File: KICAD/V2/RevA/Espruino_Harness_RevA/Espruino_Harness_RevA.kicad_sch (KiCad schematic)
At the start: 0 parts

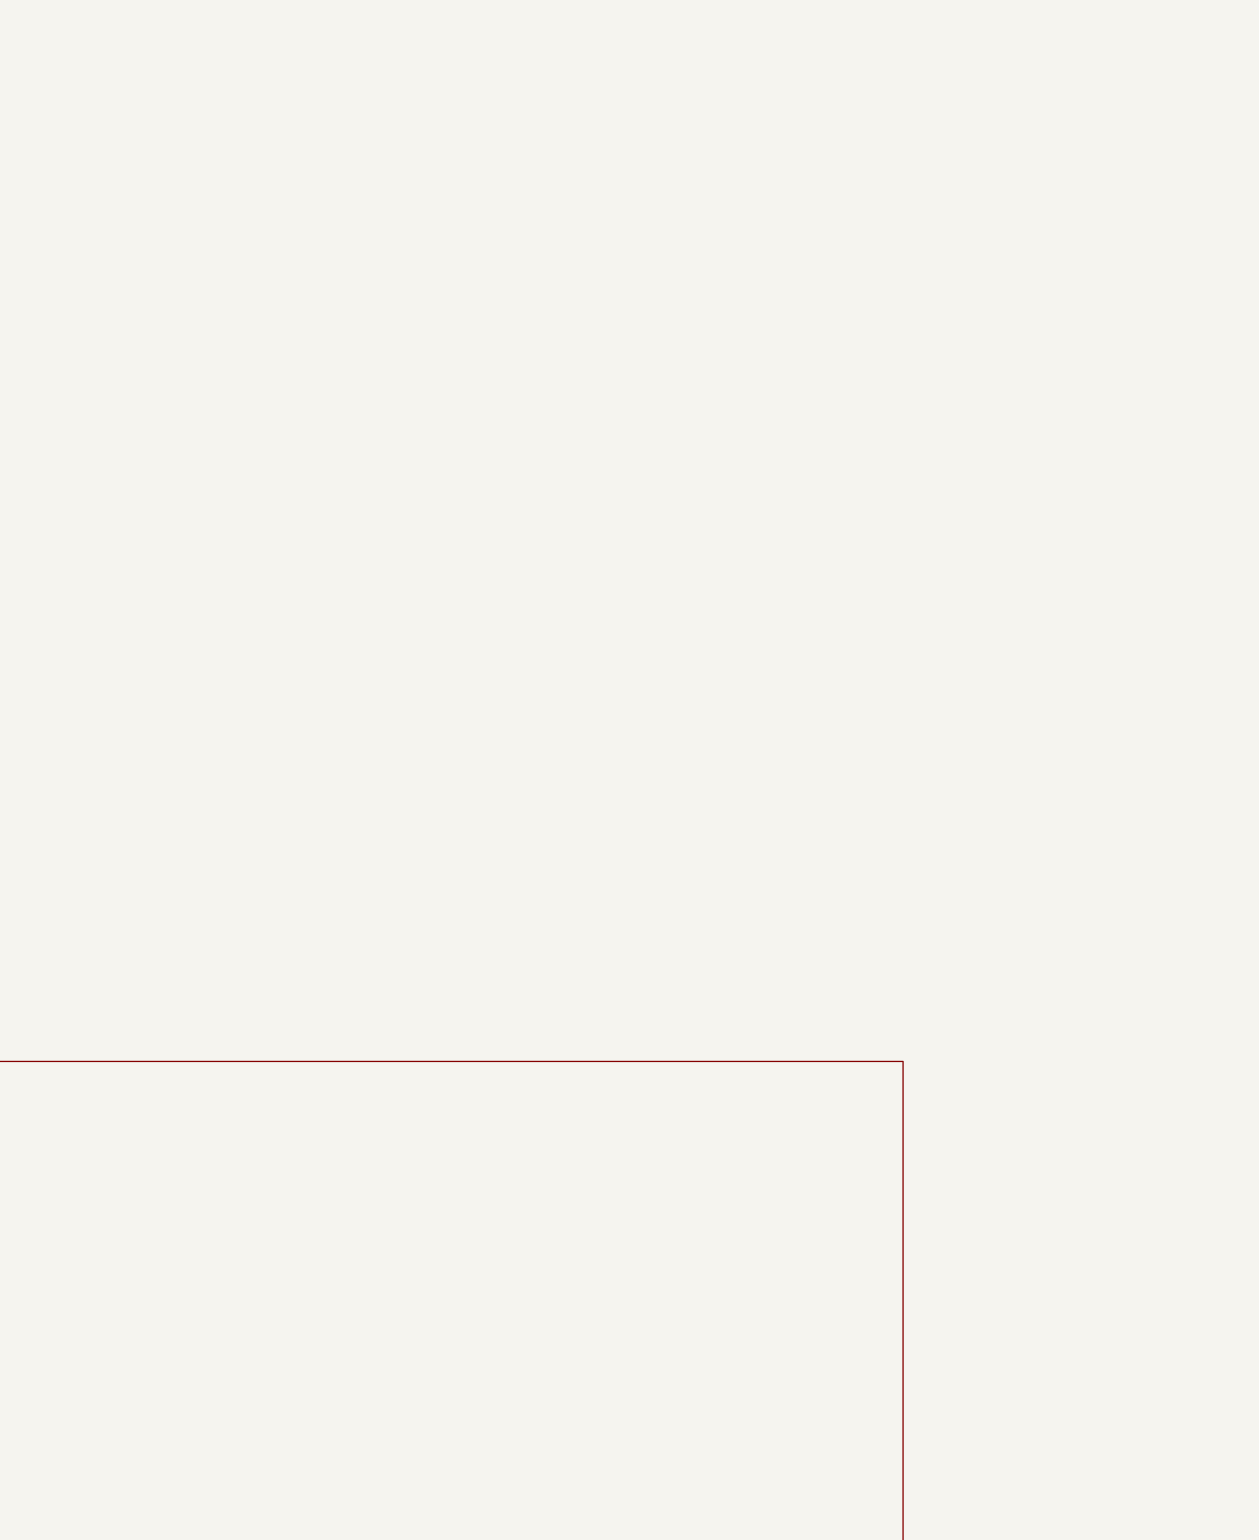
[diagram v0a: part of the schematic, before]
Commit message: Implement Target Interface and GPIO loopback
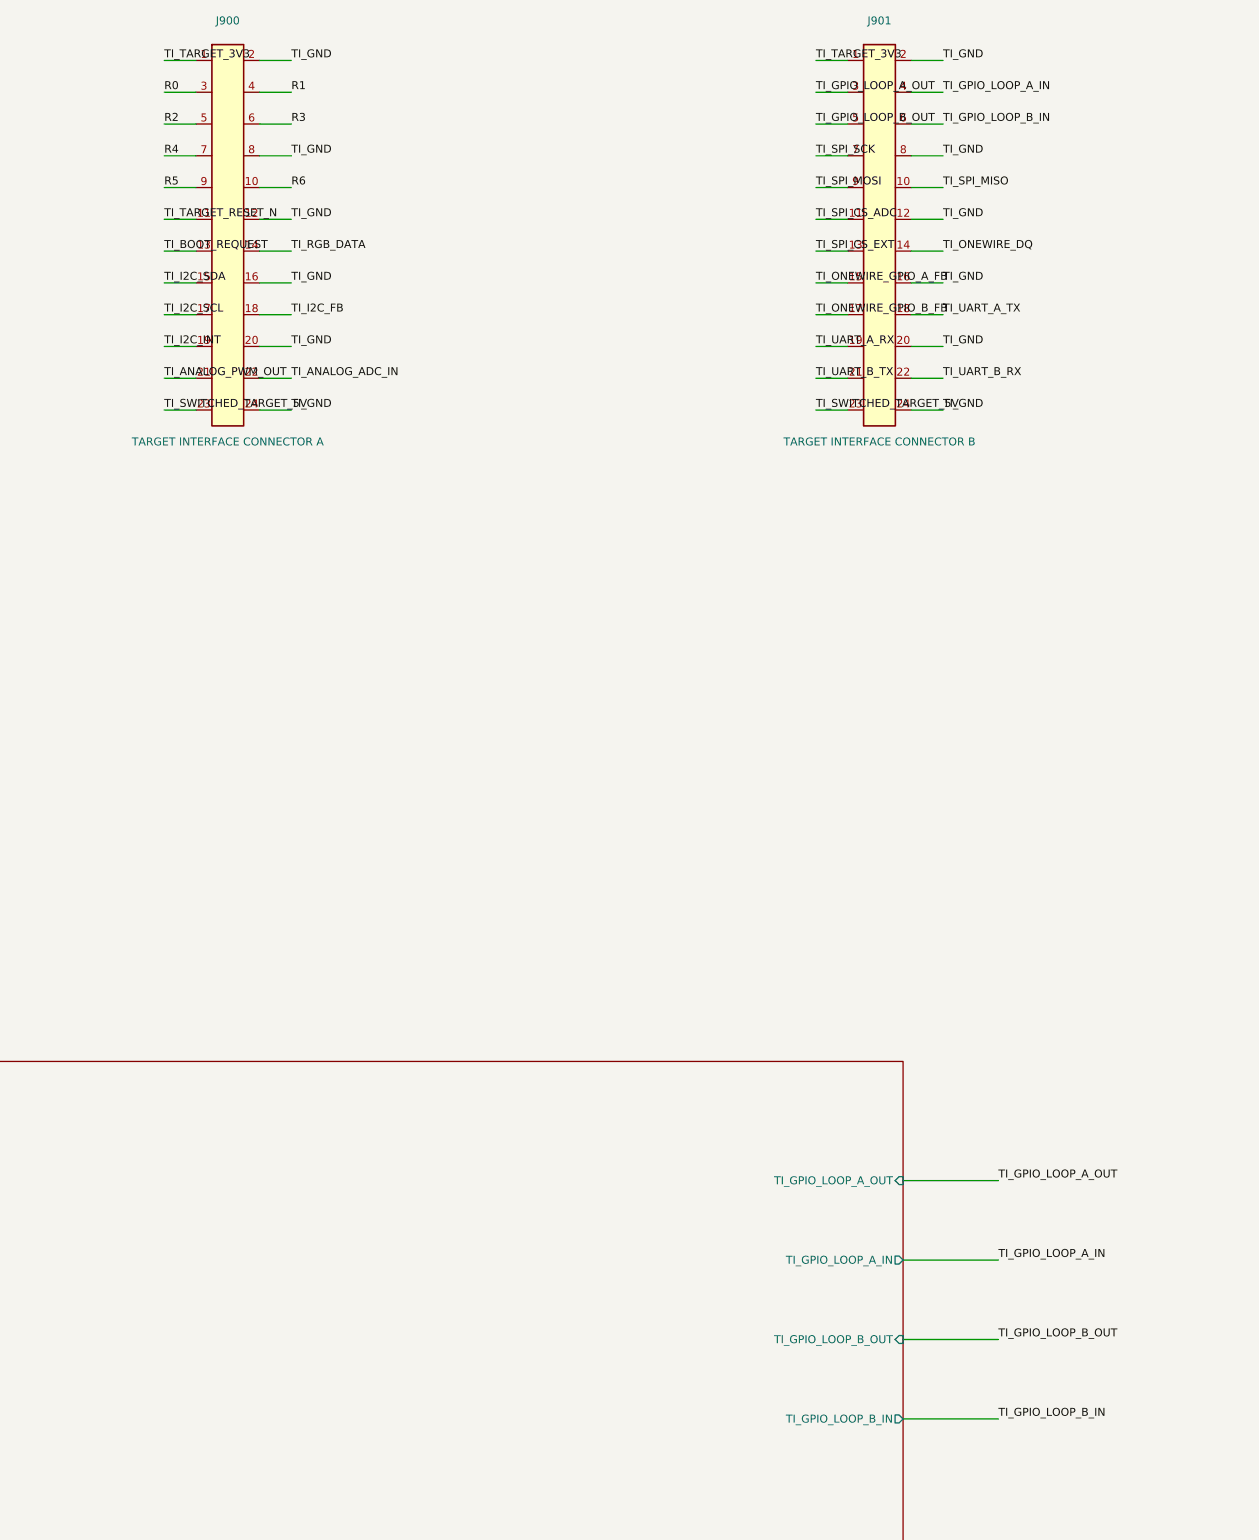
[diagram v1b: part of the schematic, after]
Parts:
- added J900: TARGET INTERFACE CONNECTOR A, symbol Espruino_Harness_RevA:Target_Interface_2x12_Odd_Even
- added J901: TARGET INTERFACE CONNECTOR B, symbol Espruino_Harness_RevA:Target_Interface_2x12_Odd_Even
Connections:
- new net R0: J900.3 (Contact_03)
- new net R1: J900.4 (Contact_04)
- new net R2: J900.5 (Contact_05)
- new net R3: J900.6 (Contact_06)
- new net R4: J900.7 (Contact_07)
- new net R5: J900.9 (Contact_09)
- new net R6: J900.10 (Contact_10)
- new net TI_ANALOG_ADC_IN: J900.22 (Contact_22)
- new net TI_ANALOG_PWM_OUT: J900.21 (Contact_21)
- new net TI_BOOT_REQUEST: J900.13 (Contact_13)
- new net TI_GND: J900.12 (Contact_12), J900.16 (Contact_16), J900.2 (Contact_02), J900.20 (Contact_20), J900.24 (Contact_24), J900.8 (Contact_08), J901.12 (Contact_12), J901.16 (Contact_16), J901.2 (Contact_02), J901.20 (Contact_20), J901.24 (Contact_24), J901.8 (Contact_08)
- new net TI_GPIO_LOOP_A_IN: J901.4 (Contact_04)
- new net TI_GPIO_LOOP_A_OUT: J901.3 (Contact_03)
- new net TI_GPIO_LOOP_B_IN: J901.6 (Contact_06)
- new net TI_GPIO_LOOP_B_OUT: J901.5 (Contact_05)
- new net TI_I2C_FB: J900.18 (Contact_18)
- new net TI_I2C_INT: J900.19 (Contact_19)
- new net TI_I2C_SCL: J900.17 (Contact_17)
- new net TI_I2C_SDA: J900.15 (Contact_15)
- new net TI_ONEWIRE_DQ: J901.14 (Contact_14)
- new net TI_ONEWIRE_GPIO_A_FB: J901.15 (Contact_15)
- new net TI_ONEWIRE_GPIO_B_FB: J901.17 (Contact_17)
- new net TI_RGB_DATA: J900.14 (Contact_14)
- new net TI_SPI_CS_ADC: J901.11 (Contact_11)
- new net TI_SPI_CS_EXT: J901.13 (Contact_13)
- new net TI_SPI_MISO: J901.10 (Contact_10)
- new net TI_SPI_MOSI: J901.9 (Contact_09)
- new net TI_SPI_SCK: J901.7 (Contact_07)
- new net TI_SWITCHED_TARGET_5V: J900.23 (Contact_23), J901.23 (Contact_23)
- new net TI_TARGET_3V3: J900.1 (Contact_01), J901.1 (Contact_01)
- new net TI_TARGET_RESET_N: J900.11 (Contact_11)
- new net TI_UART_A_RX: J901.19 (Contact_19)
- new net TI_UART_A_TX: J901.18 (Contact_18)
- new net TI_UART_B_RX: J901.22 (Contact_22)
- new net TI_UART_B_TX: J901.21 (Contact_21)
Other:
- sheet Standard_Test_Blocks ports: added TI_GPIO_LOOP_A_IN, TI_GPIO_LOOP_A_OUT, TI_GPIO_LOOP_B_IN, TI_GPIO_LOOP_B_OUT; removed none

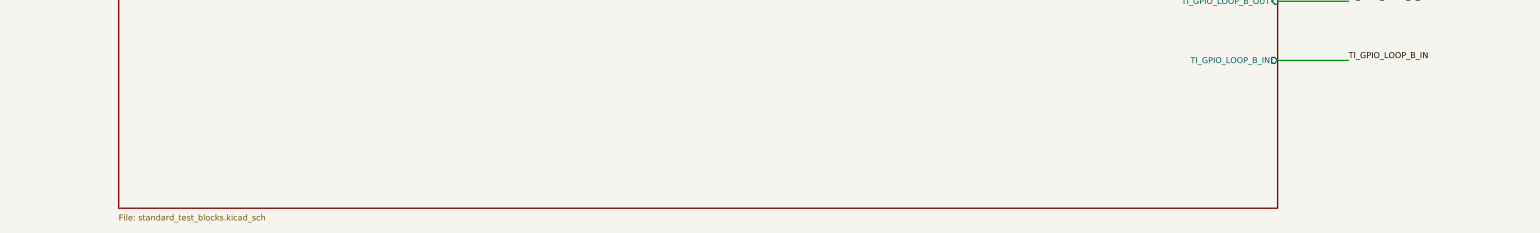
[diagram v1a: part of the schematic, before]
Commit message: Add analogue PWM feedback test block
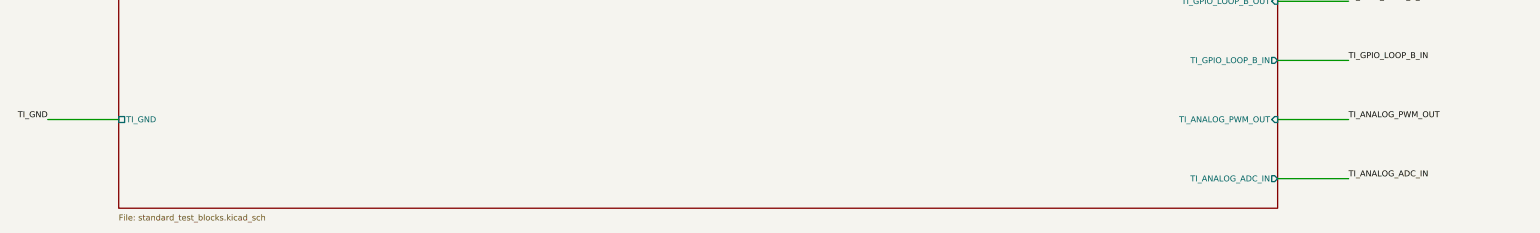
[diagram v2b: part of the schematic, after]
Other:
- sheet Standard_Test_Blocks ports: added TI_ANALOG_ADC_IN, TI_ANALOG_PWM_OUT, TI_GND; removed none
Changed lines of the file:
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@@
+		(stroke (width 0) (type default))
+	)
+	(wire
+		(pts
+			(xy 279.4 351.79) (xy 294.64 351.79)
+		)
+		(stroke (width 0) (type default))
+	)
+	(wire
+		(pts
+			(xy 279.4 364.49) (xy 294.64 364.49)
+		)
+		(stroke (width 0) (type default))
+	)
+	(wire
+		(pts
+			(xy 15.24 351.79) (xy 30.48 351.79)
+		)
 		(stroke (width 0) (type default))
 	)
@@
 		(at 294.64 339.09 0)
 		(effects (font (size 1.27 1.27)) (justify left bottom))
+	)
+	(label "TI_ANALOG_PWM_OUT"
+		(at 294.64 351.79 0)
+		(effects (font (size 1.27 1.27)) (justify left bottom))
+	)
+	(label "TI_ANALOG_ADC_IN"
+		(at 294.64 364.49 0)
+		(effects (font (size 1.27 1.27)) (justify left bottom))
+	)
+	(label "TI_GND"
+		(at 15.24 351.79 180)
+		(effects (font (size 1.27 1.27)) (justify right bottom))
 	)
 	(symbol
@@
 			(effects (font (size 1.27 1.27)) (justify right))
 		)
+		(pin "TI_ANALOG_PWM_OUT" input
+			(at 279.4 351.79 0)
+			(effects (font (size 1.27 1.27)) (justify right))
+		)
+		(pin "TI_ANALOG_ADC_IN" output
+			(at 279.4 364.49 0)
+			(effects (font (size 1.27 1.27)) (justify right))
+		)
+		(pin "TI_GND" passive
+			(at 30.48 351.79 180)
+			(effects (font (size 1.27 1.27)) (justify left))
+		)
 		(instances

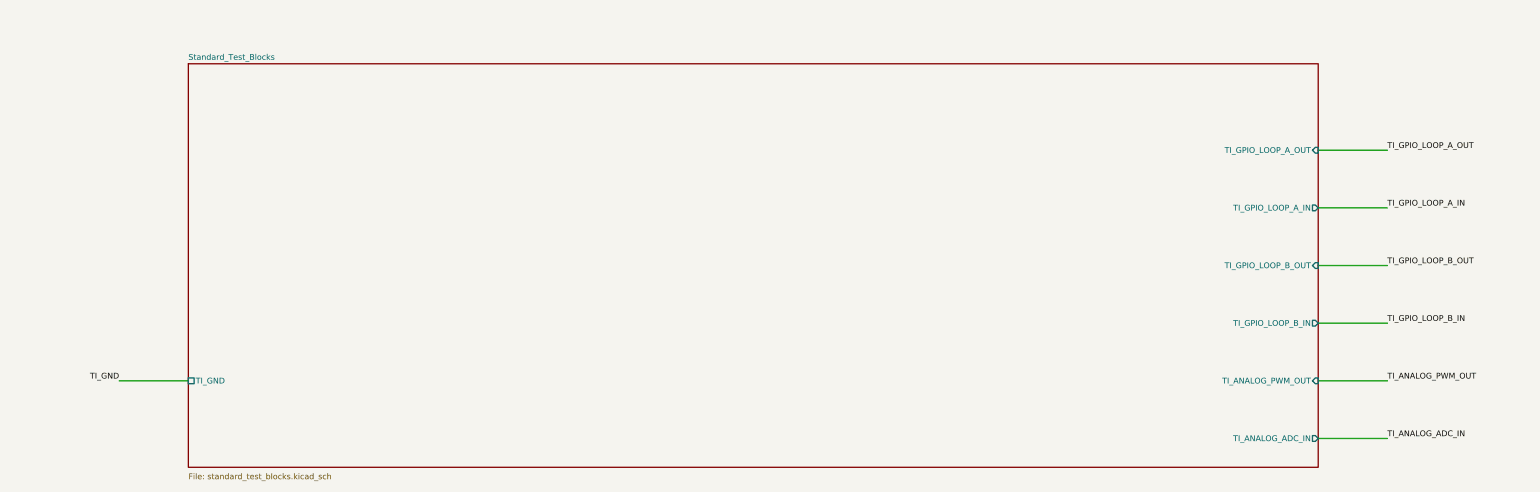
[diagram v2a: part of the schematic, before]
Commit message: Implement V2 I2C functional test block
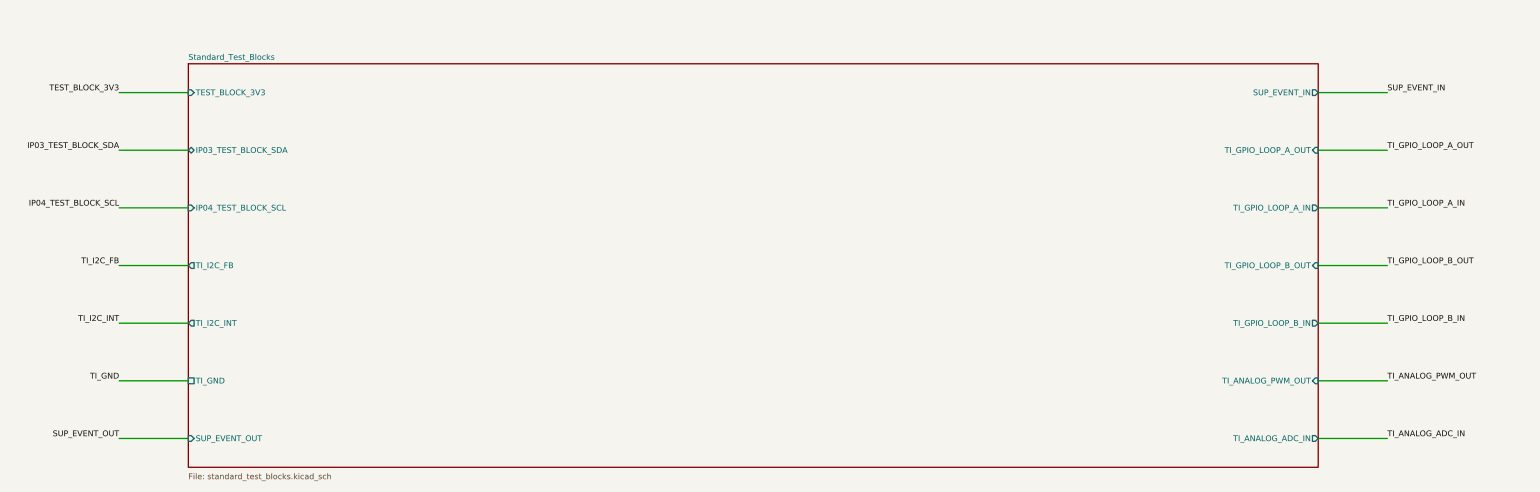
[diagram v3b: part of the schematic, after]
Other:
- sheet Standard_Test_Blocks ports: added IP03_TEST_BLOCK_SDA, IP04_TEST_BLOCK_SCL, SUP_EVENT_IN, SUP_EVENT_OUT, TEST_BLOCK_3V3, TI_I2C_FB, TI_I2C_INT; removed none
